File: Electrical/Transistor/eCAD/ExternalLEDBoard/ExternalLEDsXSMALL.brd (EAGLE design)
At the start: 19 x 27.9 mm, 7 parts

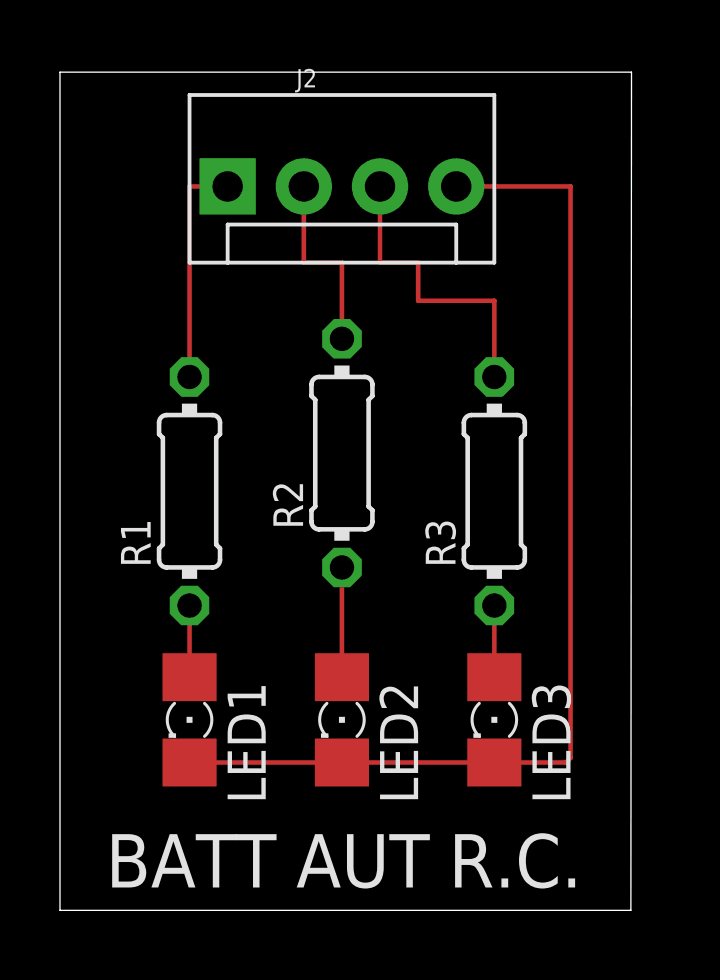
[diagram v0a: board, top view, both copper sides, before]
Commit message: Fixed DRC errors and added a copper GND plane.
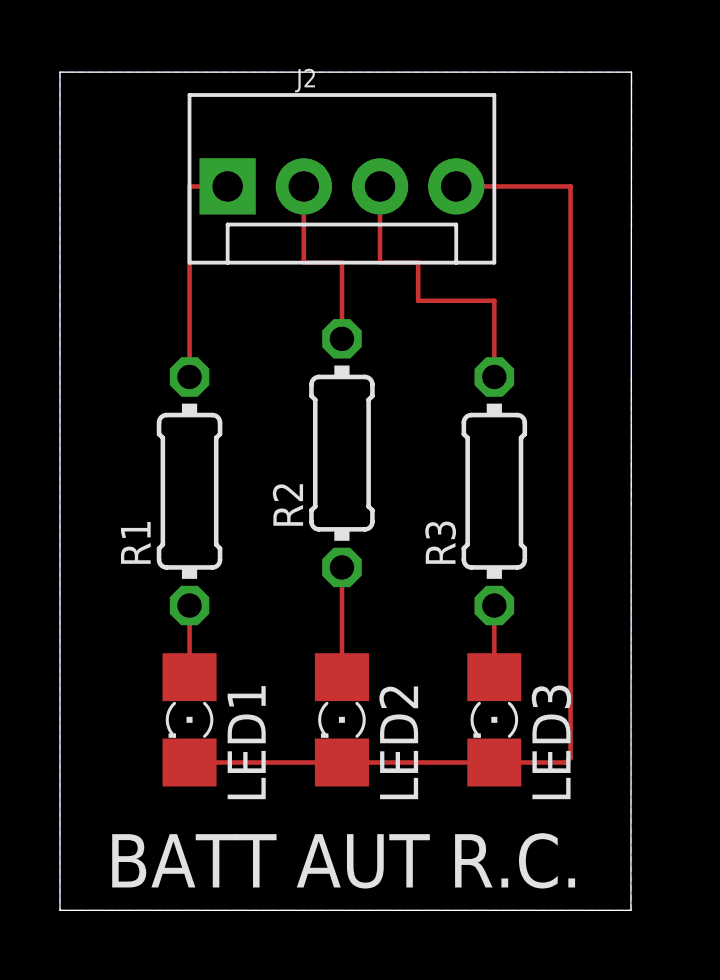
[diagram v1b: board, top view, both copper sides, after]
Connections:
- net N$7 renamed GND
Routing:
- added copper zone on layer 16, net GND
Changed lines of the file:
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@@
 <text x="101.854" y="29.972" size="1.778" layer="21">AUT</text>
 <text x="95.504" y="29.972" size="1.778" layer="21">BATT</text>
-<dimension x1="93.98" y1="57.15" x2="113.03" y2="57.15" x3="103.505" y3="58.928" textsize="1.778" layer="1" unit="inch"/>
-<dimension x1="93.98" y1="57.15" x2="93.98" y2="29.21" x3="89.662" y3="43.18" textsize="1.778" layer="1" unit="inch"/>
 <text x="107.95" y="42.164" size="1.778" layer="22" rot="MR0">IND. BD.
  REV1</text>
+<dimension x1="93.98" y1="57.15" x2="113.03" y2="57.15" x3="103.505" y3="62.738" textsize="1.778" layer="20" unit="inch"/>
+<dimension x1="93.98" y1="57.15" x2="93.98" y2="29.21" x3="88.392" y3="43.18" textsize="1.778" layer="20" unit="inch"/>
 </plain>
 <attributes>
@@
 <contactref element="R2" pad="1"/>
 <contactref element="LED2" pad="A"/>
-<wire x1="103.378" y1="40.64" x2="103.378" y2="36.83" width="0.1524" layer="1"/>
-<wire x1="103.378" y1="36.83" x2="103.378" y2="36.982" width="0" layer="19" extent="1-1"/>
+<wire x1="103.378" y1="36.83" x2="103.378" y2="40.64" width="0.1524" layer="1"/>
+<wire x1="103.378" y1="36.982" x2="103.378" y2="36.83" width="0.1524" layer="1"/>
 </signal>
 <signal name="N$6">
@@
 <contactref element="LED3" pad="A"/>
 <wire x1="108.458" y1="39.37" x2="108.458" y2="36.982" width="0.1524" layer="1"/>
-</signal>
-<signal name="N$7">
-<contactref element="LED1" pad="C"/>
-<contactref element="LED2" pad="C"/>
-<contactref element="LED3" pad="C"/>
-<contactref element="J2" pad="4"/>
-<wire x1="108.306" y1="34.138" x2="108.458" y2="34.29" width="0.1524" layer="1"/>
-<wire x1="103.378" y1="34.138" x2="108.458" y2="34.138" width="0.1524" layer="1"/>
-<wire x1="98.298" y1="34.138" x2="103.378" y2="34.138" width="0.1524" layer="1"/>
-<wire x1="108.458" y1="34.138" x2="110.846" y2="34.138" width="0.1524" layer="1"/>
-<wire x1="110.846" y1="34.138" x2="110.998" y2="34.29" width="0.1524" layer="1"/>
-<wire x1="110.998" y1="34.29" x2="110.998" y2="53.34" width="0.1524" layer="1"/>
-<wire x1="110.998" y1="53.34" x2="107.188" y2="53.34" width="0.1524" layer="1"/>
-<wire x1="108.458" y1="34.138" x2="108.306" y2="34.138" width="0" layer="19" extent="1-1"/>
 </signal>
 <signal name="N$2">
@@
 <wire x1="98.298" y1="53.34" x2="99.568" y2="53.34" width="0.1524" layer="1"/>
 </signal>
+<signal name="GND">
+<polygon width="0.1524" layer="16">
+<vertex x="93.98" y="57.15"/>
+<vertex x="93.98" y="29.21"/>
+<vertex x="113.03" y="29.21"/>
+<vertex x="113.03" y="57.15"/>
+</polygon>
+<contactref element="LED1" pad="C"/>
+<contactref element="LED2" pad="C"/>
+<contactref element="LED3" pad="C"/>
+<contactref element="J2" pad="4"/>
+<wire x1="108.306" y1="34.138" x2="108.458" y2="34.29" width="0.1524" layer="1"/>
+<wire x1="103.378" y1="34.138" x2="98.298" y2="34.138" width="0.1524" layer="1"/>
+<wire x1="110.846" y1="34.138" x2="110.998" y2="34.29" width="0.1524" layer="1"/>
+<wire x1="110.998" y1="34.29" x2="110.998" y2="53.34" width="0.1524" layer="1"/>
+<wire x1="110.998" y1="53.34" x2="107.188" y2="53.34" width="0.1524" layer="1"/>
+<wire x1="103.378" y1="34.138" x2="108.306" y2="34.138" width="0.1524" layer="1"/>
+<wire x1="110.846" y1="34.138" x2="108.458" y2="34.138" width="0.1524" layer="1"/>
+<wire x1="108.458" y1="34.138" x2="108.306" y2="34.138" width="0.1524" layer="1"/>
+</signal>
 </signals>
